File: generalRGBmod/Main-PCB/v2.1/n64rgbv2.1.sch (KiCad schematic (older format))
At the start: 89 parts, among them J11 SolderJumper_3_Open, J12 SolderJumper_3_Open, J2 SolderJumper_2_Open, J21 SolderJumper_2_Open, J3 Conn_02x05_Odd_Even, J31 SolderJumper_2_Open, U1 EPM570T100, U2 ADV7125, U3 TSH122ICT, U4 TLV70018_SOT23-5, U5 TLV70033_SOT23-5

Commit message: incremental improvements after first prototype run
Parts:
- removed FB6: Ferrite_Bead_Small, Resistor_SMD:R_0603_1608Metric, symbol Device:Ferrite_Bead_Small
- added SHIELD_FINGER1: S1761-42R, individual_footprints:Pad_4.5_3.0, symbol Connector_Generic:Conn_01x01
- C1, C2, C3, C31, C33, C34, C4, C5, C6: footprint Capacitor_SMD:C_0805_2012Metric -> Capacitor_SMD:C_0805_2012Metric_Pad1.15x1.40mm_HandSolder
- C10, C11, C12, C13, C14, C15, C16, C17, C18, C19, C20, C21, C22, C23, C24, C25, C27, C28, C32, C41, C42, C51, C52: footprint Capacitor_SMD:C_0603_1608Metric -> Capacitor_SMD:C_0603_1608Metric_Pad1.05x0.95mm_HandSolder
- FB1, FB2, FB3, FB4, FB5: value Ferrite_Bead_Small -> MPZ1608S221ATA00; footprint Resistor_SMD:R_0603_1608Metric -> Resistor_SMD:R_0603_1608Metric_Pad1.05x0.95mm_HandSolder
- J3: value Conn_02x05_Odd_Even -> 30310-6002HB
- R10, R11, R12, R13, R2, R21, R22, R31, R32, R33, R34: footprint Resistor_SMD:R_0603_1608Metric -> Resistor_SMD:R_0603_1608Metric_Pad1.05x0.95mm_HandSolder
- U4, U5: footprint Package_TO_SOT_SMD:SOT-23-5 -> Package_TO_SOT_SMD:SOT-23-5_HandSoldering
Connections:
- net Filter_Bypass: now also U1.92 (IO2_92)
- net GNDD: now also SHIELD_FINGER1.1 (Pin_1)

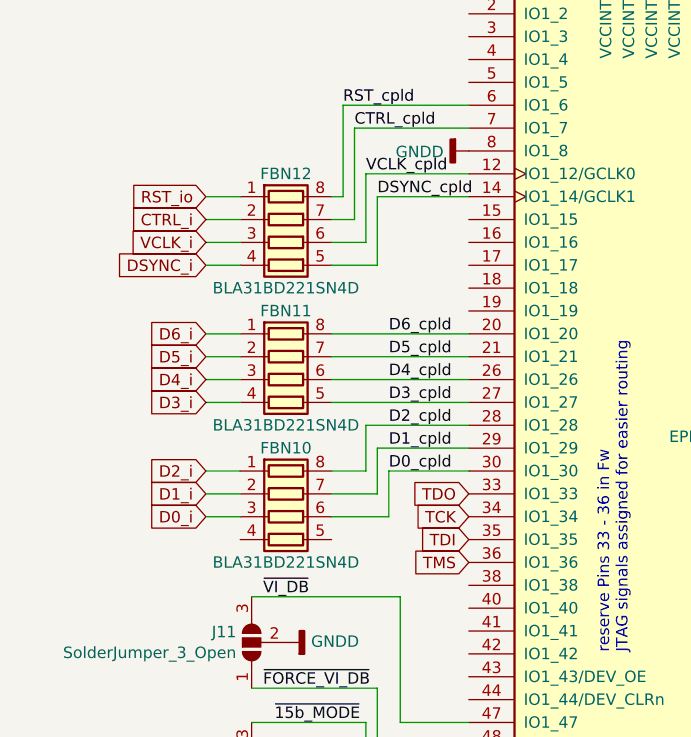
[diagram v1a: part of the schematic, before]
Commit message: update BOM for new flex cable concept
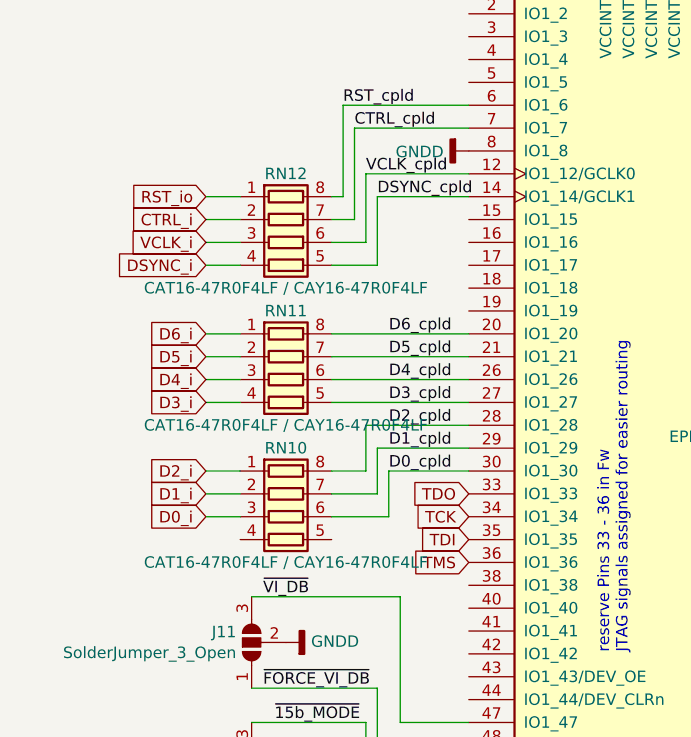
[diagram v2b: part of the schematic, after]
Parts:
- RN10: renamed from FBN10; value BLA31BD221SN4D -> CAT16-47R0F4LF / CAY16-47R0F4LF
- RN11: renamed from FBN11; value BLA31BD221SN4D -> CAT16-47R0F4LF / CAY16-47R0F4LF
- RN12: renamed from FBN12; value BLA31BD221SN4D -> CAT16-47R0F4LF / CAY16-47R0F4LF
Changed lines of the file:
@@
 $EndDescr
 $Comp
-L Device:R_Pack04 FBN11
-U 1 1 5E5D7AD4
-P 1300 5850
-F 0 "FBN11" V 1000 5850 50  0000 C CNN
-F 1 "BLA31BD221SN4D" V 1500 5850 50  0000 C CNN
-F 2 "Resistor_SMD:R_Array_Convex_4x0603" V 1575 5850 50  0001 C CNN
-F 3 "~" H 1300 5850 50  0001 C CNN
-	1    1300 5850
-	0    1    1    0
-$EndComp
-$Comp
-L Device:R_Pack04 FBN10
+L Device:R_Pack04 RN10
 U 1 1 5E5D2506
 P 1300 6450
-F 0 "FBN10" V 1000 6450 50  0000 C CNN
-F 1 "BLA31BD221SN4D" V 1500 6450 50  0000 C CNN
+F 0 "RN10" V 1000 6450 50  0000 C CNN
+F 1 "CAT16-47R0F4LF / CAY16-47R0F4LF" V 1500 6450 50  0000 C CNN
 F 2 "Resistor_SMD:R_Array_Convex_4x0603" V 1575 6450 50  0001 C CNN
 F 3 "~" H 1300 6450 50  0001 C CNN
@@
 	1700 5350 1500 5350
 $Comp
-L Device:R_Pack04 FBN12
+L Device:R_Pack04 RN12
 U 1 1 5E5D8385
 P 1300 5250
-F 0 "FBN12" V 1000 5250 50  0000 C CNN
-F 1 "BLA31BD221SN4D" V 1500 5250 50  0000 C CNN
+F 0 "RN12" V 1000 5250 50  0000 C CNN
+F 1 "CAT16-47R0F4LF / CAY16-47R0F4LF" V 1500 5250 50  0000 C CNN
 F 2 "Resistor_SMD:R_Array_Convex_4x0603" V 1575 5250 50  0001 C CNN
 F 3 "~" H 1300 5250 50  0001 C CNN
@@
 $EndComp
 Wire Bus Line
-	5150 4200 5150 7250
-Wire Bus Line
 	4800 4200 4800 7350
+Wire Bus Line
+	5150 4200 5150 7250
+$Comp
+L Device:R_Pack04 RN11
+U 1 1 5E5D7AD4
+P 1300 5850
+F 0 "RN11" V 1000 5850 50  0000 C CNN
+F 1 "CAT16-47R0F4LF / CAY16-47R0F4LF" V 1500 5850 50  0000 C CNN
+F 2 "Resistor_SMD:R_Array_Convex_4x0603" V 1575 5850 50  0001 C CNN
+F 3 "~" H 1300 5850 50  0001 C CNN
+	1    1300 5850
+	0    1    1    0
+$EndComp
 $EndSCHEMATC

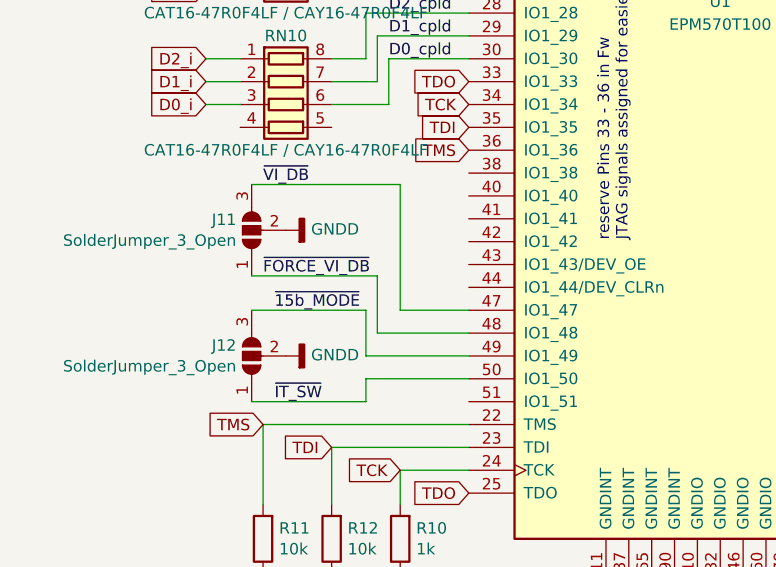
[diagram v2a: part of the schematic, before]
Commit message: remove auto deblur stuff from N64RGB - I found more and more situations where the auto detection does not work reliable - so I removed it for now
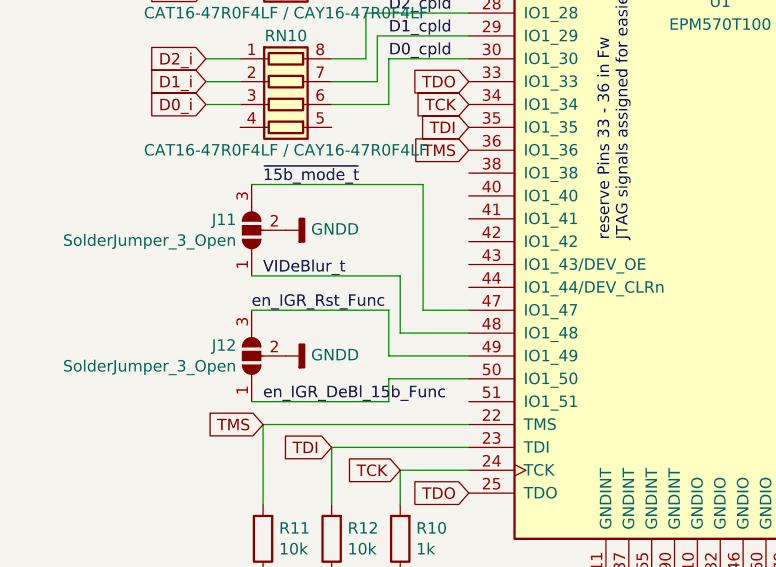
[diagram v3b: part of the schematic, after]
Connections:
- net ~15b_MODE renamed en_IGR_Rst_Func
- net ~FORCE_VI_DB renamed VIDeBlur_t
- net ~IT_SW renamed en_IGR_DeBl_15b_Func
- net ~VI_DB renamed ~15b_mode_t
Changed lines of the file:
@@
 EESchema Schematic File Version 4
-EELAYER 30 0
+LIBS:n64rgbv2.1-cache
+EELAYER 29 0
 EELAYER END
 $Descr A4 8268 11693 portrait
@@
 $EndComp
 Wire Wire Line
-	1700 7200 1150 7200
+	1800 7200 1150 7200
 Wire Wire Line
-	1800 6800 1150 6800
+	1900 6800 1150 6800
 $Comp
 L power:GNDD #PWR0160
@@
 $EndComp
 Text Label 1200 7200 0    50   ~ 0
-~FORCE_VI_DB
+VIDeBlur_t
 Text Label 1200 6800 0    50   ~ 0
-~VI_DB
+~15b_mode_t
 $Comp
 L power:GNDD #PWR0161
@@
 $EndComp
 Wire Wire Line
-	1150 7350 1650 7350
+	1150 7350 1750 7350
 Wire Wire Line
-	1650 7350 1650 7550
-Text Label 1250 7750 0    50   ~ 0
-~IT_SW
-Text Label 1250 7350 0    50   ~ 0
-~15b_MODE
+	1750 7350 1750 7550
+Text Label 1200 7750 0    50   ~ 0
+en_IGR_DeBl_15b_Func
+Text Label 1150 7350 0    50   ~ 0
+en_IGR_Rst_Func
 $Comp
 L n64rgbv2.1-rescue:TLV70018_SOT23-5-Regulator_Linear U4
@@
 reserve Pins 33 - 36 in Fw\nJTAG signals assigned for easier routing\n
 Wire Wire Line
-	1150 7750 1650 7750
+	1150 7750 1750 7750
 Wire Wire Line
-	2100 7550 1650 7550
+	2100 7550 1750 7550
 Wire Wire Line
-	2100 7650 1650 7650
+	2100 7650 1750 7650
 Wire Wire Line
-	1650 7650 1650 7750
+	1750 7650 1750 7750
 Wire Wire Line
-	2100 7450 1700 7450
+	2100 7450 1800 7450
 Wire Wire Line
-	1700 7450 1700 7200
+	1800 7450 1800 7200
 Wire Wire Line
-	2100 7350 1800 7350
-Wire Wire Line
-	1800 6800 1800 7350
+	2100 7350 1900 7350
 Text GLabel 4300 7550 2    50   Input ~ 0
 Filter_Bypass
@@
 	0    1    1    0
 $EndComp
-Wire Bus Line
-	4800 4200 4800 7350
-Wire Bus Line
-	5150 4200 5150 7250
 $Comp
 L Device:R_Pack04 RN11
@@
 	0    1    1    0
 $EndComp
+Wire Wire Line
+	1900 6800 1900 7350
+Wire Bus Line
+	5150 4200 5150 7250
+Wire Bus Line
+	4800 4200 4800 7350
 $EndSCHEMATC

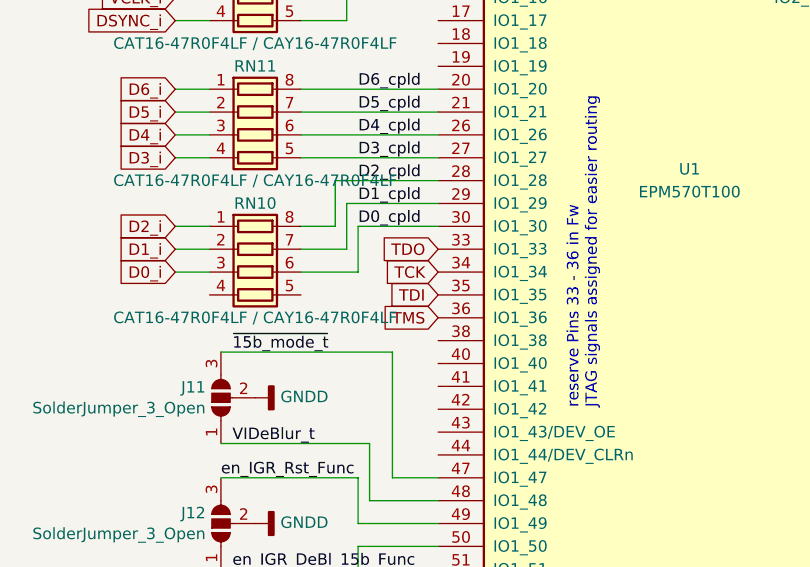
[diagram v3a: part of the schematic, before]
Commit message: do not run JTAG through other pins as this may cause problem if used CPLDs are assembled
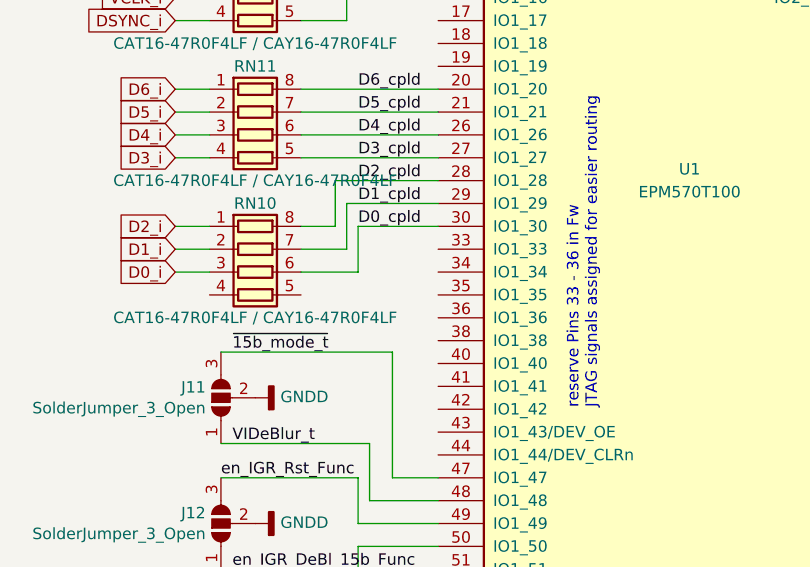
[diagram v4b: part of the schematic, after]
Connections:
- net TCK: no longer U1.34 (IO1_34)
- net TDI: no longer U1.35 (IO1_35)
- net TDO: no longer U1.33 (IO1_33)
- net TMS: no longer U1.36 (IO1_36)
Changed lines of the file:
@@
 EESchema Schematic File Version 4
-LIBS:n64rgbv2.1-cache
-EELAYER 29 0
+EELAYER 30 0
 EELAYER END
 $Descr A4 8268 11693 portrait
@@
 	1    0    0    -1
 $EndComp
-Text GLabel 2100 6550 0    50   Input ~ 0
-TDI
-Text GLabel 2100 6450 0    50   Input ~ 0
-TCK
-Text GLabel 2100 6350 0    50   Input ~ 0
-TDO
-Text GLabel 2100 6650 0    50   Input ~ 0
-TMS
 Text Notes 2800 7050 1    50   ~ 0
 reserve Pins 33 - 36 in Fw\nJTAG signals assigned for easier routing\n
